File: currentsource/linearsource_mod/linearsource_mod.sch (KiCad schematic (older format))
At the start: 16 parts, among them P1 CONN_01X04, P2 CONN_01X04, Q1 Q_NMOS_DGS, Q2 BC546, U1 LM358

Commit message: currentsource: Prettify schematic for v2
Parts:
- C1, C2: footprint (none) -> Capacitors_SMD:C_1206
- P1, P2: footprint (none) -> Pin_Headers:Pin_Header_Straight_1x04
- Q1: value Q_NMOS_DGS -> PSMN017-30BL; footprint (none) -> TO_SOT_Packages_SMD:TO-263-3Lead
- Q2: value BC546 -> BC849; footprint TO-92 -> TO_SOT_Packages_SMD:SOT-323; symbol BC546 -> BC849
- R1, R2, R3, R4, R6, R7, R8, R9: footprint (none) -> Resistors_SMD:R_1206
- R5: footprint (none) -> Resistors_SMD:R_2512
- U1: footprint (none) -> SMD_Packages:SOIC-8-N
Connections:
- wire segments 50 -> 59
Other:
- moved on the sheet: C1, C2, P1, P2, Q1, R1, R2, R3, R4, R5, R6, R7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

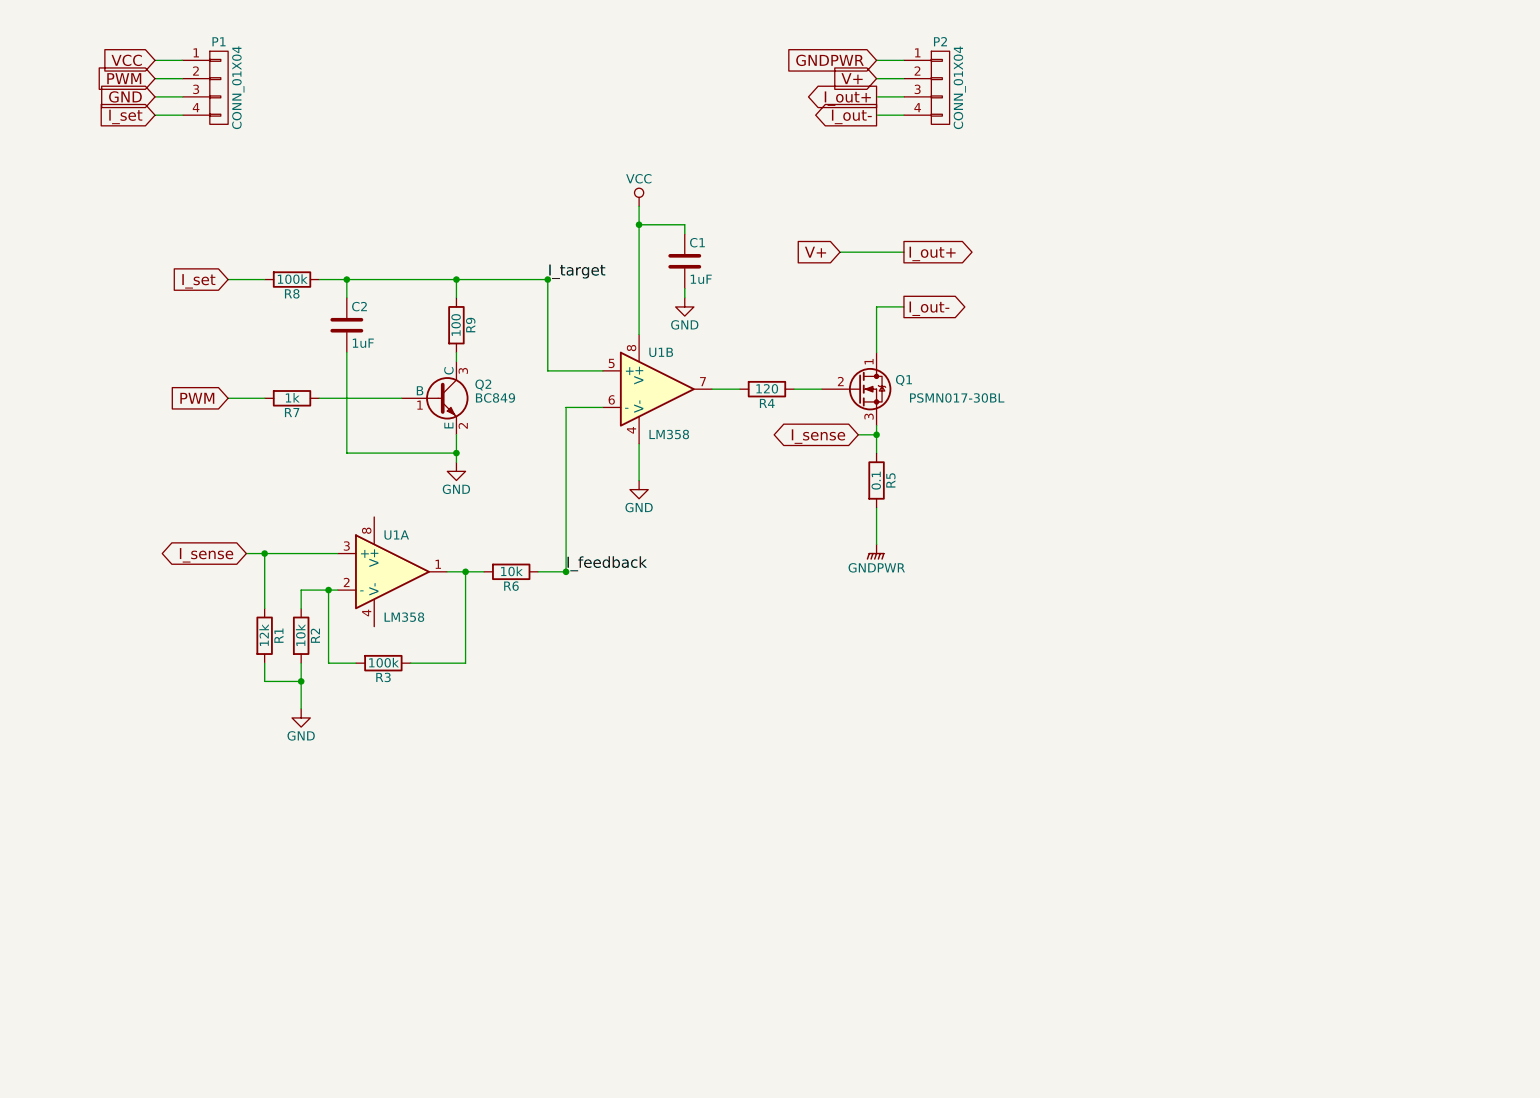
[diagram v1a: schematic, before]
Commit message: currentsource: Fix ERC
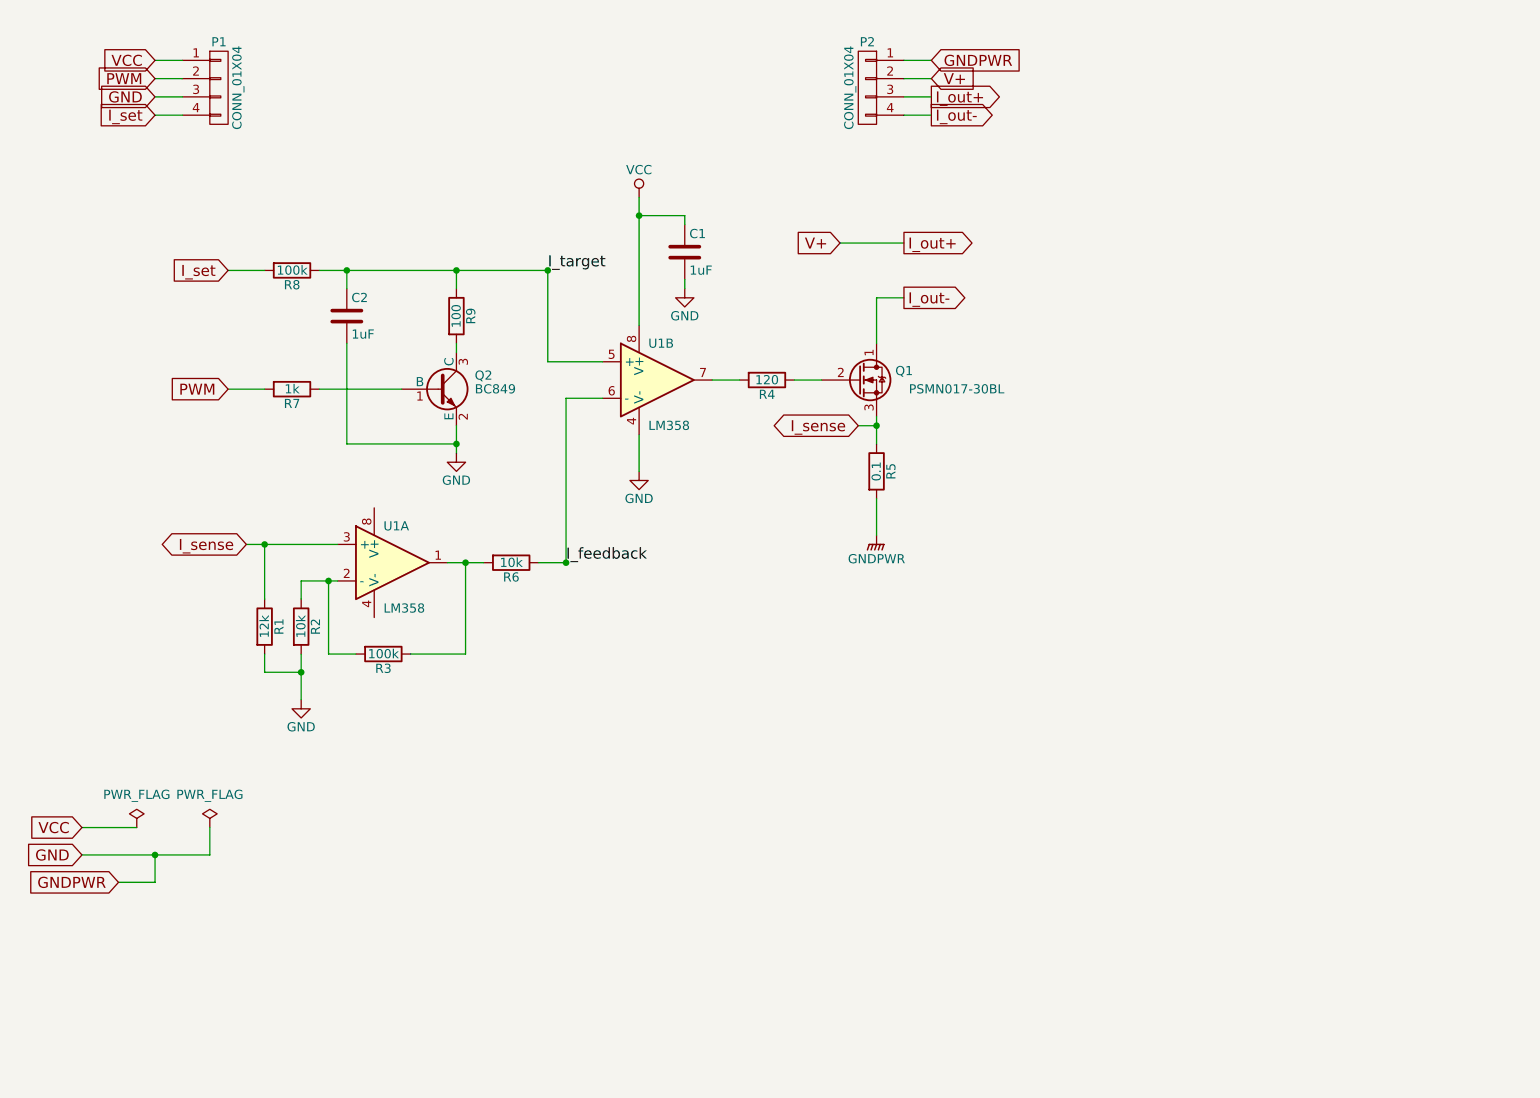
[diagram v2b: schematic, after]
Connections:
- net GNDPWR is gone; now on net GND: P2.1 (P1), R5.2
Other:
- moved on the sheet: C1, C2, P2, Q1, Q2, R1, R2, R3, R4, R5, R6, R7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

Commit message: currentsource: Start of routing tracks
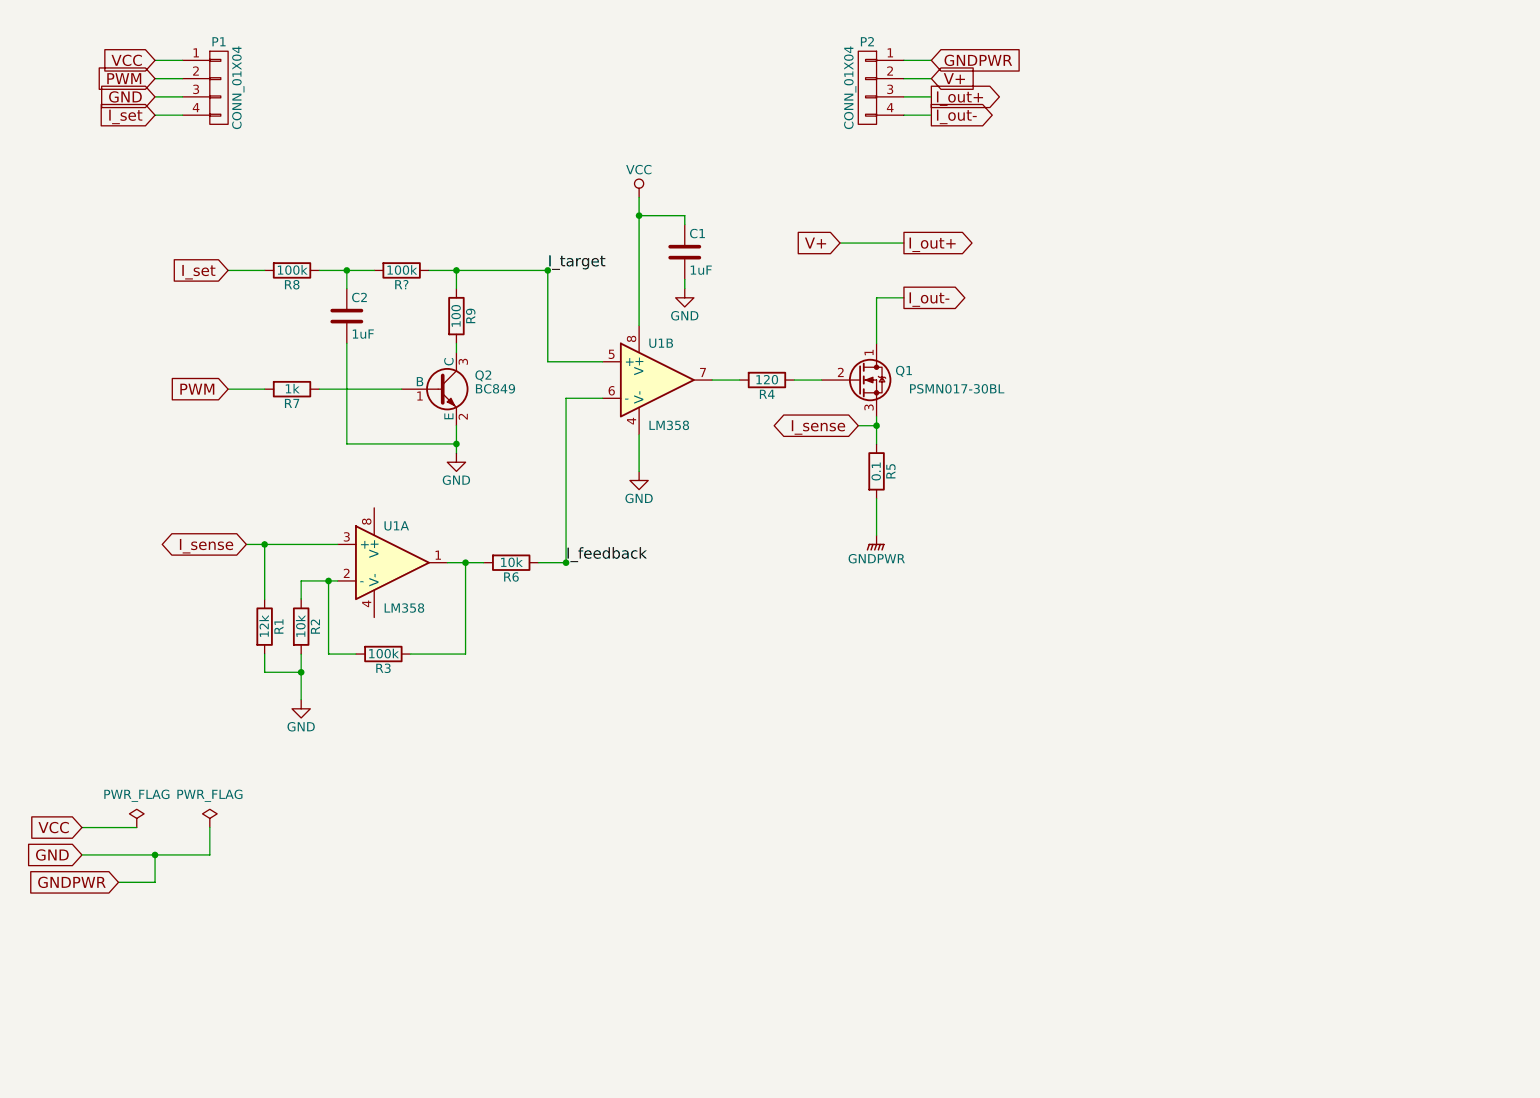
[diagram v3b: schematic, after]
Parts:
- added R?: 100k, symbol R
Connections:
- net I_target: now also R?.1; no longer C2.1, R8.1
- new net: C2.1, R8.1, R?.2
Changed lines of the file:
@@
 LIBS:contrib
 LIBS:valves
+LIBS:linearsource_mod-cache
 EELAYER 25 0
 EELAYER END
@@
 	2900 4100 2900 3600
 Wire Wire Line
-	2000 3700 2150 3700
-Wire Wire Line
-	2150 3700 2200 3700
+	2000 3700 2200 3700
 Wire Wire Line
 	2000 3700 2000 3800
@@
 $EndComp
 Wire Wire Line
-	3850 1600 3850 1700
-Wire Wire Line
-	3850 1700 3850 2300
+	3850 1600 3850 2300
 Wire Wire Line
 	4700 2600 4850 2600
 Wire Wire Line
-	5150 2800 5150 2850
-Wire Wire Line
-	5150 2850 5150 2950
+	5150 2800 5150 2950
 Wire Wire Line
 	5150 3250 5150 3450
 Connection ~ 5150 2850
 Wire Wire Line
-	2000 4100 2000 4200
-Wire Wire Line
-	2000 4200 2000 4350
+	2000 4100 2000 4350
 Wire Wire Line
 	1800 3800 1800 3500
 Wire Wire Line
-	1700 3500 1800 3500
-Wire Wire Line
-	1800 3500 2200 3500
+	1700 3500 2200 3500
 Wire Wire Line
 	1800 4100 1800 4200
@@
 	4250 2600 4400 2600
 Wire Wire Line
-	2800 3600 2900 3600
-Wire Wire Line
-	2900 3600 3000 3600
+	2800 3600 3000 3600
 $Comp
 L R R6
@@
 $EndComp
 Wire Wire Line
-	2850 2850 2850 2950
-Wire Wire Line
-	2850 2950 2850 3000
+	2850 2850 2850 3000
 Wire Wire Line
 	2850 2450 2850 2400
@@
 	3350 2500 3650 2500
 Wire Wire Line
-	2100 2000 2250 2000
-Wire Wire Line
-	2250 2000 2850 2000
-Wire Wire Line
-	2850 2000 3350 2000
+	2100 2000 2400 2000
+Wire Wire Line
+	2700 2000 3350 2000
 Wire Wire Line
 	3350 2000 3350 2500
@@
 $EndComp
 Wire Wire Line
-	2250 2000 2250 2000
-Wire Wire Line
 	2250 2000 2250 2100
 Connection ~ 2250 2000
@@
 	1100 5050 800  5050
 Wire Wire Line
-	1500 5050 1500 5200
-Wire Wire Line
-	1500 5200 1200 5200
-Wire Wire Line
-	1200 5200 800  5200
+	1500 5200 1500 5050
+Wire Wire Line
+	800  5200 1500 5200
 Wire Wire Line
 	1000 5350 1200 5350
@@
 	1200 5350 1200 5200
 Connection ~ 1200 5200
+$Comp
+L R R?
+U 1 1 59871E1C
+P 2550 2000
+F 0 "R?" V 2630 2000 50  0000 C CNN
+F 1 "100k" V 2550 2000 50  0000 C CNN
+F 2 "" V 2480 2000 50  0001 C CNN
+F 3 "" H 2550 2000 50  0001 C CNN
+	1    2550 2000
+	0    1    1    0
+$EndComp
 $EndSCHEMATC

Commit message: currentsource: Add testpoint for Itarget
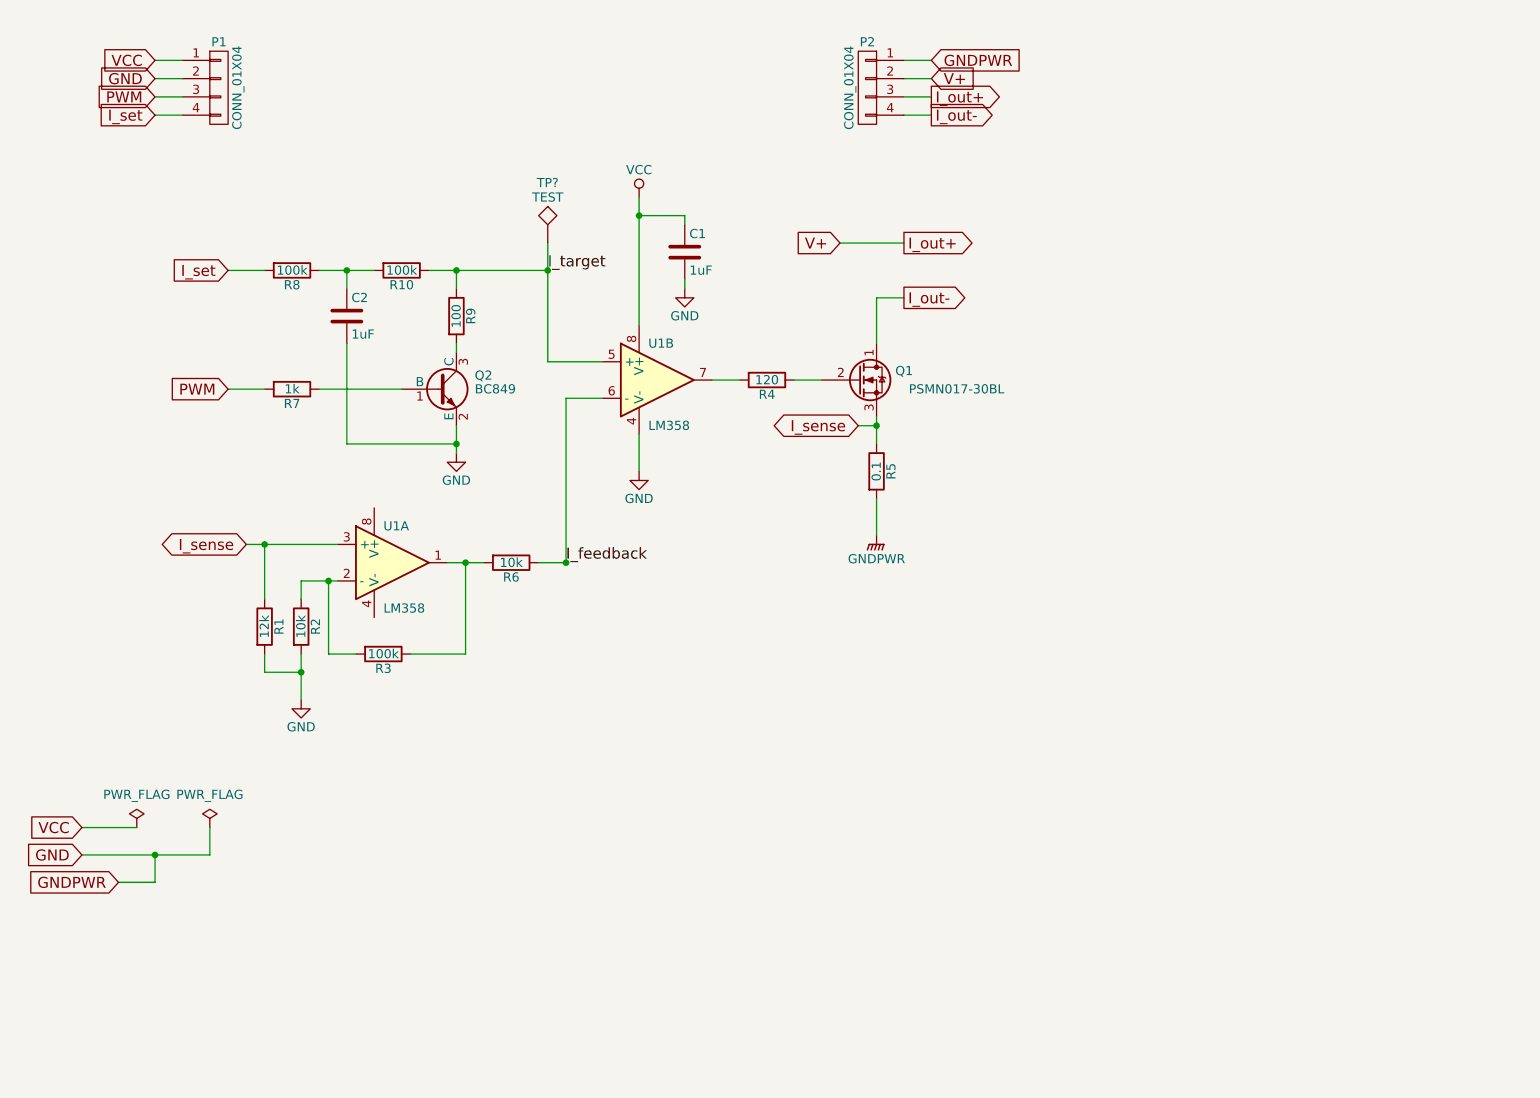
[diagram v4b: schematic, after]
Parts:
- added TP?: TEST, symbol TEST
- R10: renamed from R?; footprint (none) -> Resistors_SMD:R_1206
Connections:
- net GND: now also P1.2 (P2); no longer P1.3 (P3)
- net I_target: now also TP?.1
- net PWM: now also P1.3 (P3); no longer P1.2 (P2)
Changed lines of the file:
@@
 	2900 4100 2900 3600
 Wire Wire Line
-	2000 3700 2200 3700
+	2000 3700 2150 3700
+Wire Wire Line
+	2150 3700 2200 3700
 Wire Wire Line
 	2000 3700 2000 3800
@@
 $EndComp
 Wire Wire Line
-	3850 1600 3850 2300
+	3850 1600 3850 1700
+Wire Wire Line
+	3850 1700 3850 2300
 Wire Wire Line
 	4700 2600 4850 2600
 Wire Wire Line
-	5150 2800 5150 2950
+	5150 2800 5150 2850
+Wire Wire Line
+	5150 2850 5150 2950
 Wire Wire Line
 	5150 3250 5150 3450
 Connection ~ 5150 2850
 Wire Wire Line
-	2000 4100 2000 4350
+	2000 4100 2000 4200
+Wire Wire Line
+	2000 4200 2000 4350
 Wire Wire Line
 	1800 3800 1800 3500
 Wire Wire Line
-	1700 3500 2200 3500
+	1700 3500 1800 3500
+Wire Wire Line
+	1800 3500 2200 3500
 Wire Wire Line
 	1800 4100 1800 4200
@@
 	4250 2600 4400 2600
 Wire Wire Line
-	2800 3600 3000 3600
+	2800 3600 2900 3600
+Wire Wire Line
+	2900 3600 3000 3600
 $Comp
 L R R6
@@
 Text GLabel 1200 850  0    60   Input ~ 0
 VCC
+Text GLabel 1200 1050 0    60   Input ~ 0
+PWM
 Text GLabel 1200 950  0    60   Input ~ 0
-PWM
-Text GLabel 1200 1050 0    60   Input ~ 0
 GND
 Text GLabel 1200 1150 0    60   Input ~ 0
@@
 	1200 850  1350 850
 Wire Wire Line
-	1200 950  1350 950
-Wire Wire Line
-	1200 1050 1350 1050
-Wire Wire Line
 	1200 1150 1350 1150
 $Comp
@@
 $EndComp
 Wire Wire Line
-	2850 2850 2850 3000
+	2850 2850 2850 2950
+Wire Wire Line
+	2850 2950 2850 3000
 Wire Wire Line
 	2850 2450 2850 2400
@@
 	3350 2500 3650 2500
 Wire Wire Line
-	2100 2000 2400 2000
-Wire Wire Line
-	2700 2000 3350 2000
+	2100 2000 2250 2000
+Wire Wire Line
+	2250 2000 2400 2000
+Wire Wire Line
+	2700 2000 2850 2000
+Wire Wire Line
+	2850 2000 3350 2000
+Wire Wire Line
+	3350 1850 3350 2000
 Wire Wire Line
 	3350 2000 3350 2500
@@
 	1500 5200 1500 5050
 Wire Wire Line
-	800  5200 1500 5200
+	800  5200 1200 5200
+Wire Wire Line
+	1200 5200 1500 5200
 Wire Wire Line
 	1000 5350 1200 5350
@@
 Connection ~ 1200 5200
 $Comp
-L R R?
+L R R10
 U 1 1 59871E1C
 P 2550 2000
-F 0 "R?" V 2630 2000 50  0000 C CNN
+F 0 "R10" V 2630 2000 50  0000 C CNN
 F 1 "100k" V 2550 2000 50  0000 C CNN
-F 2 "" V 2480 2000 50  0001 C CNN
+F 2 "Resistors_SMD:R_1206" V 2480 2000 50  0001 C CNN
 F 3 "" H 2550 2000 50  0001 C CNN
 	1    2550 2000
 	0    1    1    0
 $EndComp
+Wire Wire Line
+	1200 1050 1350 1050
+Wire Wire Line
+	1200 950  1350 950
+$Comp
+L TEST TP?
+U 1 1 598733DB
+P 3350 1850
+F 0 "TP?" H 3350 2150 50  0000 C BNN
+F 1 "TEST" H 3350 2100 50  0000 C CNN
+F 2 "" H 3350 1850 50  0001 C CNN
+F 3 "" H 3350 1850 50  0001 C CNN
+	1    3350 1850
+	1    0    0    -1
+$EndComp
 $EndSCHEMATC
